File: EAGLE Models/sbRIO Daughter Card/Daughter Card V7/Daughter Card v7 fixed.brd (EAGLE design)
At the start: 136.7 x 102.9 mm, 92 parts, among them IC1 BTS716G, IC10 MIC5225-3.3YM5-TR, IC11 MIC5225-3.3YM5-TR, IC12 MIC5225-3.3YM5-TR, IC2 BTS716G, IC3 BTS716G, IC4 ADXL345, IC5 L3G4200D, IC8 MIC5225-3.3YM5-TR, IC9 MIC5225-3.3YM5-TR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

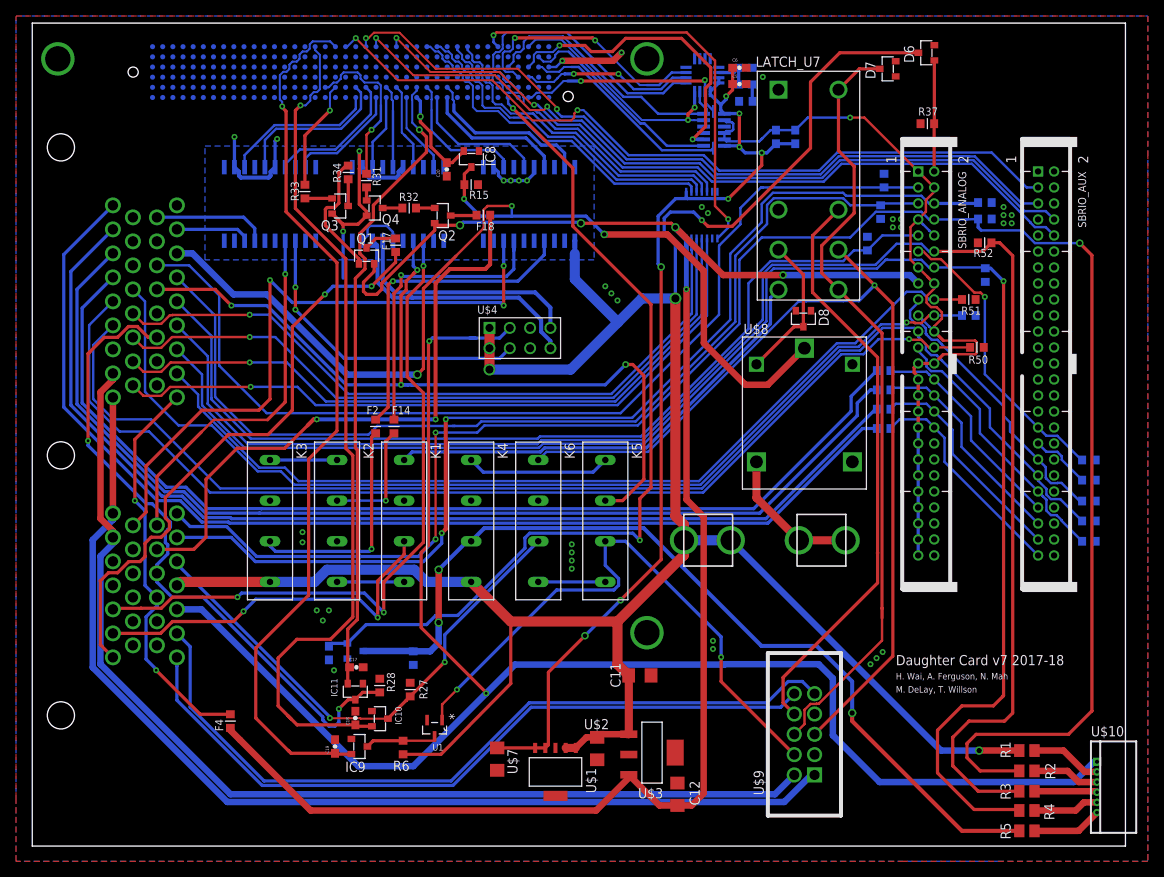
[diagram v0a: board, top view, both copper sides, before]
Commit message: began to fix dfm issues
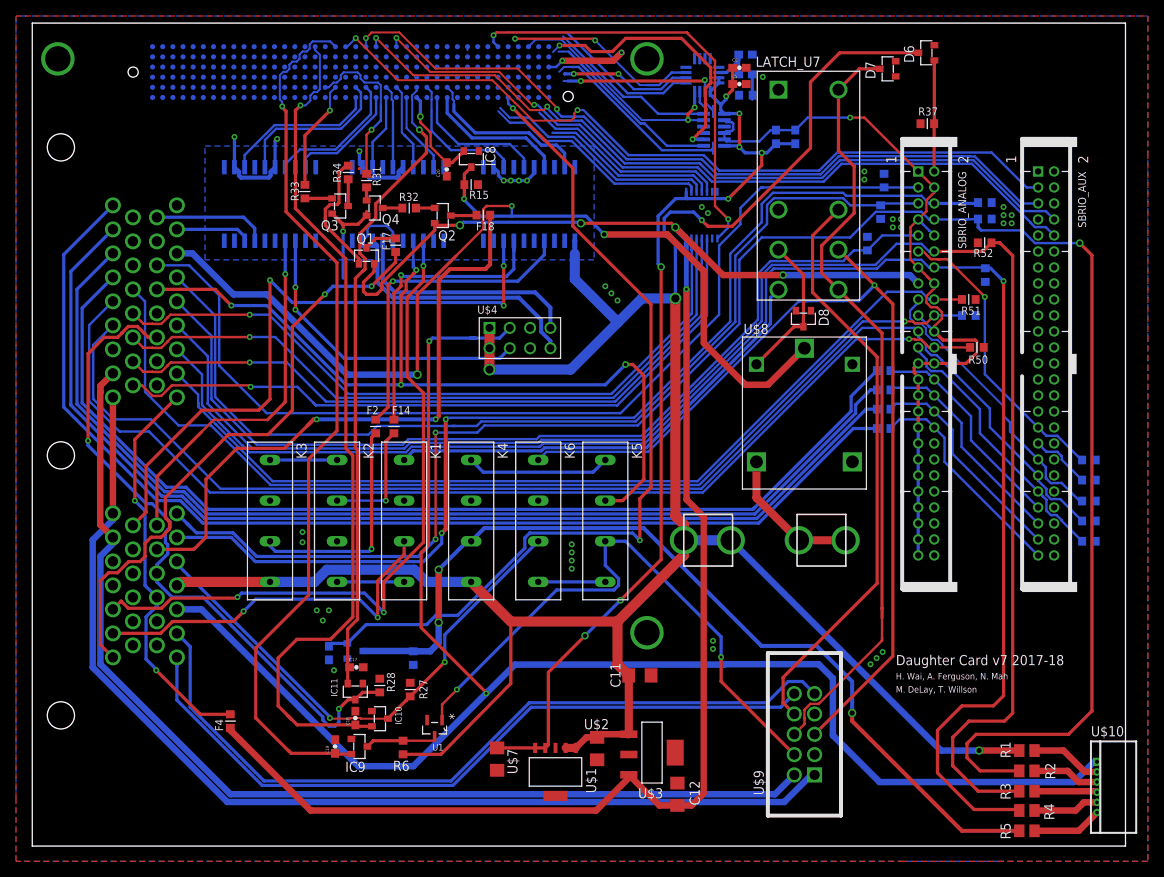
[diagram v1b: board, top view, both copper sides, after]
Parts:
- moved C14 1.65 mm to (89.2, 98.9)
- moved C13 1.27 mm to (89.2, 96.5)
- moved R38 0.76 mm to (89.2, 93.9)
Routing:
- net DIO86: track 41.0 -> 22.3 mm
- net DIO88: track 43.3 -> 28.7 mm
- net DIO85: track 40.6 -> 26.2 mm
- net DIO87: track 42.7 -> 29.5 mm
- net DIO32: track 36.0 -> 26.1 mm
- net DIO18: track 34.3 -> 24.9 mm
- net GND: track 62.5 -> 54.6 mm, vias 43 -> 45
- net DIO65: track 31.8 -> 24.5 mm
- net DIO0: track 27.3 -> 22.1 mm
- net DIO64: track 21.8 -> 16.6 mm
- net DIO17: track 38.2 -> 33.9 mm
- net DIO48: track 39.6 -> 36.1 mm
- net DIO16: track 26.8 -> 24.0 mm
- net PO3: track 107.4 -> 105.6 mm
- net N$11: track 2.11 -> 3.53 mm
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
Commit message: continued fixing dfm issues
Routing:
- net DIO86: track 22.3 -> 41.5 mm
- net DIO88: track 28.7 -> 42.9 mm
- net DIO85: track 26.2 -> 40.0 mm
- net DIO87: track 29.5 -> 43.1 mm
- net DIO32: track 26.1 -> 36.1 mm
- net DIO18: track 24.9 -> 34.5 mm
- net DIO65: track 24.5 -> 31.5 mm
- net DIO0: track 22.1 -> 27.3 mm
- net DIO64: track 16.6 -> 21.8 mm
- net DIO17: track 33.9 -> 38.2 mm
- net DIO48: track 36.1 -> 39.6 mm
- net DIO16: track 24.0 -> 26.9 mm
- net DIO95: track 107.2 -> 105.7 mm
- net DIO45: track 20.7 -> 21.8 mm
- net DIO41: track 10.3 -> 11.1 mm

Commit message: finished making all gerbers. Ready to send out
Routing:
- net DIO48: track 39.6 -> 26.7 mm
- net DIO1: track 109.2 -> 111.9 mm
- net GND: track 54.6 -> 56.9 mm
- net BMS_CAN_H: track 92.8 -> 91.7 mm
- net LATCH_SW_OUT: track 119.5 -> 118.6 mm
- net SIGNAL_GND: track 199.0 -> 198.3 mm
- net DIO92: track 97.1 -> 96.4 mm
- net N$9: track 136.6 -> 137.2 mm
- net DIO42: track 17.3 -> 17.8 mm
